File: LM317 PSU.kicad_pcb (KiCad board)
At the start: 2 copper layers, 137.5 x 90 mm, 63 parts, among them J1 4MM Red female, J2 4MM Black female, J3 Barrel_Jack_MountingPin, J4 Conn_01x07_Male, J5 Conn_01x07_Female, J6 Conn_01x01_Female, J7 Conn_01x01_Female, J8 V- jumper, Q1 2N2222, SW1 SW_Push_SPDT, U1 NA555, U2 TL061, U3 LM358, U4 LM317_3PinPackage, U5 LM358, U6 7905

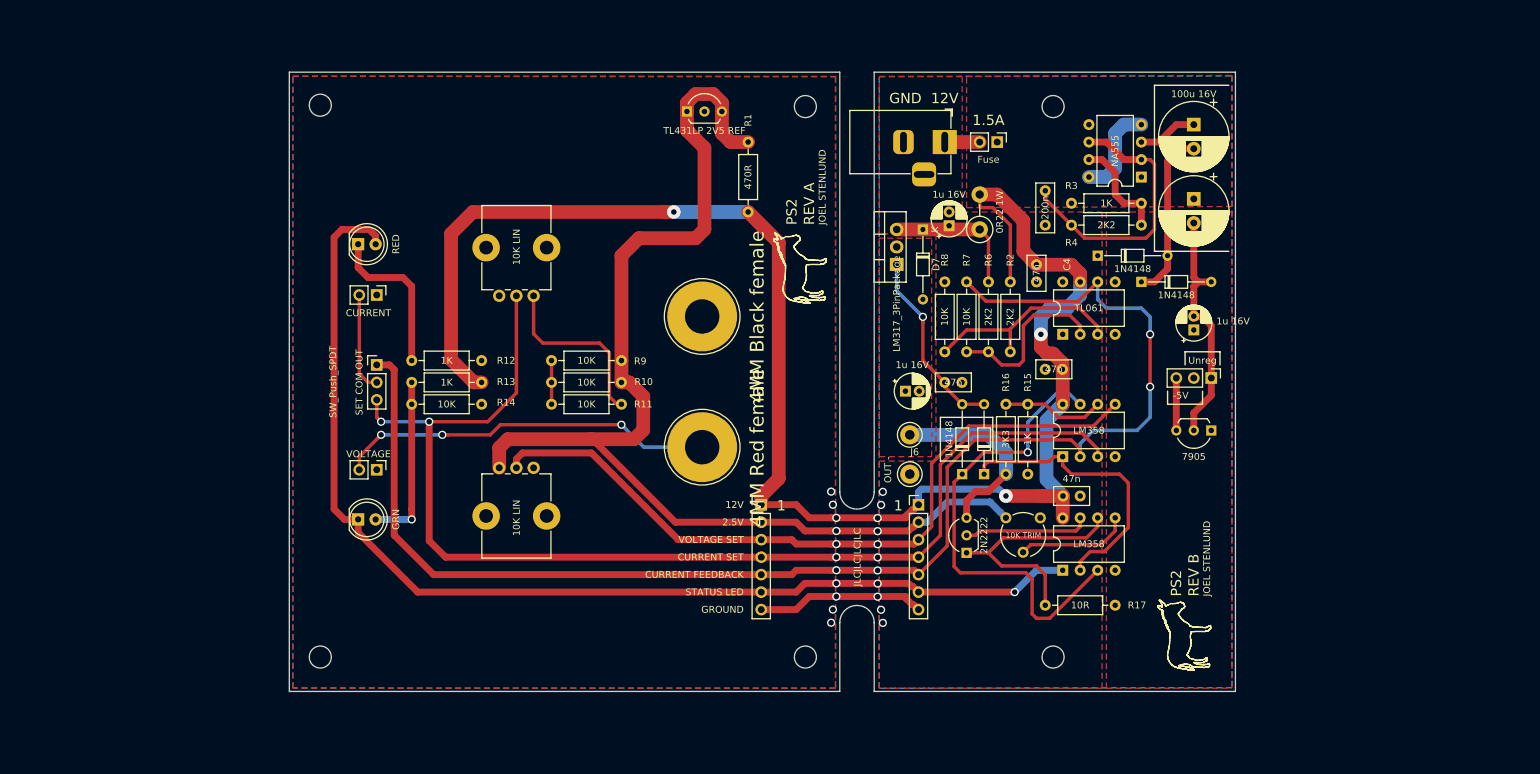
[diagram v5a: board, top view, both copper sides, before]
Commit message: fixed broken silkscreen
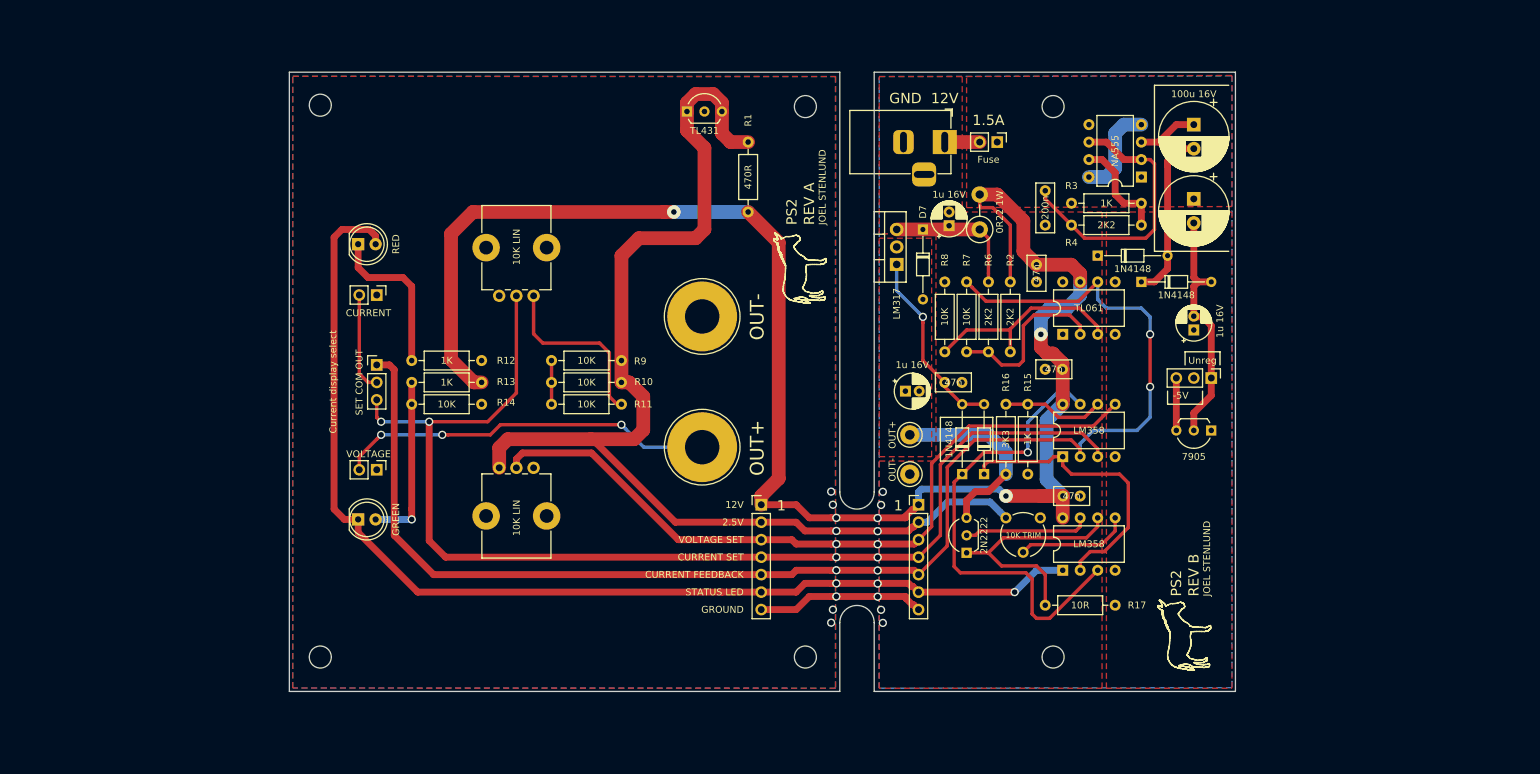
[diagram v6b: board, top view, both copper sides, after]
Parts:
- D1: value TL431LP 2V5 REF -> TL431
- D4: value GRN -> GREEN
- J1: value 4MM Red female -> OUT+
- J2: value 4MM Black female -> OUT-
- SW1: value SW_Push_SPDT -> Current display select
- U4: value LM317_3PinPackage -> LM317
- renumbered J6 to OUT+
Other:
- board text removed: "JLCJLCJLCJLC"
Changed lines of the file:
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@@
   (general
     (thickness 1.6)
-    (drawings 2361)
+    (drawings 2360)
     (tracks 406)
     (zones 0)
@@
     (visible_elements 7FFFFFFF)
     (pcbplotparams
-      (layerselection 0x010fc_ffffffff)
+      (layerselection 0x010f0_ffffffff)
       (usegerberextensions false)
       (usegerberattributes false)
@@
       (drillshape 0)
       (scaleselection 1)
-      (outputdirectory "REV_A_GRBR/"))
+      (outputdirectory "REV_B_GRBR/"))
   )
   (net 0 "")
@@
       (effects (font (size 1 1) (thickness 0.15)))
     )
-    (fp_text value "1u 16V" (at 1.27 5.715) (layer F.SilkS)
+    (fp_text value "1u 16V" (at 1.27 3.81 90) (layer F.SilkS)
       (effects (font (size 1 1) (thickness 0.15)))
     )
@@
     (descr "Diode, DO-34_SOD68 series, Axial, Horizontal, pin pitch=10.16mm, , length*diameter=3.04*1.6mm^2, , https://www.nxp.com/docs/en/data-sheet/KTY83_SER.pdf")
     (tags "Diode DO-34_SOD68 series Axial Horizontal pin pitch 10.16mm  length 3.04mm diameter 1.6mm")
-    (fp_text reference D7 (at 5.08 -1.92 270) (layer F.SilkS)
+    (fp_text reference D7 (at -2.54 0 270) (layer F.SilkS)
       (effects (font (size 1 1) (thickness 0.15)))
     )
@@
       (effects (font (size 1 1) (thickness 0.15)))
     )
-    (fp_line (start 3.56 -0.8) (end 3.56 0.8) (layer F.Fab) (width 0.1))
-    (fp_line (start 3.56 0.8) (end 6.6 0.8) (layer F.Fab) (width 0.1))
-    (fp_line (start 6.6 0.8) (end 6.6 -0.8) (layer F.Fab) (width 0.1))
-    (fp_line (start 6.6 -0.8) (end 3.56 -0.8) (layer F.Fab) (width 0.1))
-    (fp_line (start 0 0) (end 3.56 0) (layer F.Fab) (width 0.1))
-    (fp_line (start 10.16 0) (end 6.6 0) (layer F.Fab) (width 0.1))
-    (fp_line (start 4.016 -0.8) (end 4.016 0.8) (layer F.Fab) (width 0.1))
-    (fp_line (start 4.116 -0.8) (end 4.116 0.8) (layer F.Fab) (width 0.1))
-    (fp_line (start 3.916 -0.8) (end 3.916 0.8) (layer F.Fab) (width 0.1))
-    (fp_line (start 3.44 -0.92) (end 3.44 0.92) (layer F.SilkS) (width 0.12))
-    (fp_line (start 3.44 0.92) (end 6.72 0.92) (layer F.SilkS) (width 0.12))
-    (fp_line (start 6.72 0.92) (end 6.72 -0.92) (layer F.SilkS) (width 0.12))
-    (fp_line (start 6.72 -0.92) (end 3.44 -0.92) (layer F.SilkS) (width 0.12))
-    (fp_line (start 0.99 0) (end 3.44 0) (layer F.SilkS) (width 0.12))
-    (fp_line (start 9.17 0) (end 6.72 0) (layer F.SilkS) (width 0.12))
-    (fp_line (start 4.016 -0.92) (end 4.016 0.92) (layer F.SilkS) (width 0.12))
-    (fp_line (start 4.136 -0.92) (end 4.136 0.92) (layer F.SilkS) (width 0.12))
-    (fp_line (start 3.896 -0.92) (end 3.896 0.92) (layer F.SilkS) (width 0.12))
-    (fp_line (start -1 -1.05) (end -1 1.05) (layer F.CrtYd) (width 0.05))
-    (fp_line (start -1 1.05) (end 11.16 1.05) (layer F.CrtYd) (width 0.05))
-    (fp_line (start 11.16 1.05) (end 11.16 -1.05) (layer F.CrtYd) (width 0.05))
-    (fp_line (start 11.16 -1.05) (end -1 -1.05) (layer F.CrtYd) (width 0.05))
-    (fp_text user %R (at 5.308 0 270) (layer F.Fab)
-      (effects (font (size 0.608 0.608) (thickness 0.0912)))
-    )
     (fp_text user K (at 0 -1.75 270) (layer F.Fab)
       (effects (font (size 1 1) (thickness 0.15)))
     )
-    (fp_text user K (at 0 -1.75 270) (layer F.SilkS)
+    (fp_text user K (at 0 -1.75 270) (layer F.Fab)
       (effects (font (size 1 1) (thickness 0.15)))
     )
-    (pad 1 thru_hole rect (at 0 0 270) (size 1.5 1.5) (drill 0.75) (layers *.Cu *.Mask)
-      (net 7 /REG_INP))
+    (fp_text user %R (at 5.308 0 270) (layer F.Fab)
+      (effects (font (size 0.608 0.608) (thickness 0.0912)))
+    )
+    (fp_line (start 11.16 -1.05) (end -1 -1.05) (layer F.CrtYd) (width 0.05))
+    (fp_line (start 11.16 1.05) (end 11.16 -1.05) (layer F.CrtYd) (width 0.05))
+    (fp_line (start -1 1.05) (end 11.16 1.05) (layer F.CrtYd) (width 0.05))
+    (fp_line (start -1 -1.05) (end -1 1.05) (layer F.CrtYd) (width 0.05))
+    (fp_line (start 3.896 -0.92) (end 3.896 0.92) (layer F.SilkS) (width 0.12))
+    (fp_line (start 4.136 -0.92) (end 4.136 0.92) (layer F.SilkS) (width 0.12))
+    (fp_line (start 4.016 -0.92) (end 4.016 0.92) (layer F.SilkS) (width 0.12))
+    (fp_line (start 9.17 0) (end 6.72 0) (layer F.SilkS) (width 0.12))
+    (fp_line (start 0.99 0) (end 3.44 0) (layer F.SilkS) (width 0.12))
+    (fp_line (start 6.72 -0.92) (end 3.44 -0.92) (layer F.SilkS) (width 0.12))
+    (fp_line (start 6.72 0.92) (end 6.72 -0.92) (layer F.SilkS) (width 0.12))
+    (fp_line (start 3.44 0.92) (end 6.72 0.92) (layer F.SilkS) (width 0.12))
+    (fp_line (start 3.44 -0.92) (end 3.44 0.92) (layer F.SilkS) (width 0.12))
+    (fp_line (start 3.916 -0.8) (end 3.916 0.8) (layer F.Fab) (width 0.1))
+    (fp_line (start 4.116 -0.8) (end 4.116 0.8) (layer F.Fab) (width 0.1))
+    (fp_line (start 4.016 -0.8) (end 4.016 0.8) (layer F.Fab) (width 0.1))
+    (fp_line (start 10.16 0) (end 6.6 0) (layer F.Fab) (width 0.1))
+    (fp_line (start 0 0) (end 3.56 0) (layer F.Fab) (width 0.1))
+    (fp_line (start 6.6 -0.8) (end 3.56 -0.8) (layer F.Fab) (width 0.1))
+    (fp_line (start 6.6 0.8) (end 6.6 -0.8) (layer F.Fab) (width 0.1))
+    (fp_line (start 3.56 0.8) (end 6.6 0.8) (layer F.Fab) (width 0.1))
+    (fp_line (start 3.56 -0.8) (end 3.56 0.8) (layer F.Fab) (width 0.1))
     (pad 2 thru_hole oval (at 10.16 0 270) (size 1.5 1.5) (drill 0.75) (layers *.Cu *.Mask)
       (net 9 OUTPUT))
+    (pad 1 thru_hole rect (at 0 0 270) (size 1.5 1.5) (drill 0.75) (layers *.Cu *.Mask)
+      (net 7 /REG_INP))
     (model ${KISYS3DMOD}/Diode_THT.3dshapes/D_DO-34_SOD68_P10.16mm_Horizontal.wrl
       (at (xyz 0 0 0))
@@
     (descr "wire loop with bead as test point, loop diameter 3.5mm, hole diameter 1.4mm")
     (tags "test point wire loop bead")
-    (fp_text reference J6 (at 0.7 2.5) (layer F.SilkS)
+    (fp_text reference OUT+ (at -2.54 0 90) (layer F.SilkS)
       (effects (font (size 1 1) (thickness 0.15)))
     )
@@
       (effects (font (size 1 1) (thickness 0.15)))
     )
-    (fp_text value "4MM Black female" (at 8 0.06 90) (layer F.SilkS)
+    (fp_text value OUT- (at 8 0.06 90) (layer F.SilkS)
       (effects (font (size 2 2) (thickness 0.5)))
     )
@@
       (effects (font (size 1 1) (thickness 0.15)))
     )
-    (fp_text value "4MM Red female" (at 8 0.11 90) (layer F.SilkS)
+    (fp_text value OUT+ (at 8 0.11 90) (layer F.SilkS)
       (effects (font (size 2 2) (thickness 0.5)))
     )
@@
       (effects (font (size 1 1) (thickness 0.15)))
     )
-    (fp_text user "OUT -" (at -3.175 -0.635 90) (layer F.SilkS)
+    (fp_text user OUT- (at -2.54 -0.635 90) (layer F.SilkS)
       (effects (font (size 1 1) (thickness 0.15)))
     )
@@
     (descr "C, Disc series, Radial, pin pitch=2.50mm, , diameter*width=5*2.5mm^2, Capacitor, http://cdn-reichelt.de/documents/datenblatt/B300/DS_KERKO_TC.pdf")
     (tags "C Disc series Radial pin pitch 2.50mm  diameter 5mm width 2.5mm Capacitor")
-    (fp_text reference C4 (at 2.54 4.445 90) (layer F.SilkS)
+    (fp_text reference C4 (at 2.54 4.445 90) (layer F.Fab)
       (effects (font (size 1 1) (thickness 0.15)))
     )
@@
       (effects (font (size 1 1) (thickness 0.15)))
     )
-    (fp_text value 47n (at 1.25 2.5) (layer F.SilkS)
+    (fp_text value 47n (at 1.25 0) (layer F.SilkS)
       (effects (font (size 1 1) (thickness 0.15)))
     )
@@
       (effects (font (size 1 1) (thickness 0.15)))
     )
-    (fp_text value "TL431LP 2V5 REF" (at 2.54 2.79) (layer F.SilkS)
+    (fp_text value TL431 (at 2.54 2.79) (layer F.SilkS)
       (effects (font (size 1 1) (thickness 0.15)))
     )
@@
       (effects (font (size 1 1) (thickness 0.15)))
     )
-    (fp_text value GRN (at 5.5 0 90) (layer F.SilkS)
+    (fp_text value GREEN (at 5.5 0 90) (layer F.SilkS)
       (effects (font (size 1 1) (thickness 0.15)))
     )
@@
       (effects (font (size 1 1) (thickness 0.15)))
     )
-    (fp_text value SW_Push_SPDT (at -6.35 2.455 90) (layer F.SilkS)
+    (fp_text value "Current display select" (at -6.35 2.455 90) (layer F.SilkS)
       (effects (font (size 1 1) (thickness 0.2)))
     )
@@
       (effects (font (size 1 1) (thickness 0.15)))
     )
-    (fp_text value LM317_3PinPackage (at -5.715 0 270) (layer F.SilkS)
+    (fp_text value LM317 (at -5.715 0 270) (layer F.SilkS)
       (effects (font (size 1 1) (thickness 0.15)))
     )
@@
     (effects (font (size 1 1) (thickness 0.15)))
   )
-  (gr_text JLCJLCJLCJLC (at 142.555 90.485 90) (layer F.SilkS)
-    (effects (font (size 1 1) (thickness 0.15)))
-  )
